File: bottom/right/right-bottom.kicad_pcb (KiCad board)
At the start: 2 copper layers, 171 x 95 mm, 6 parts

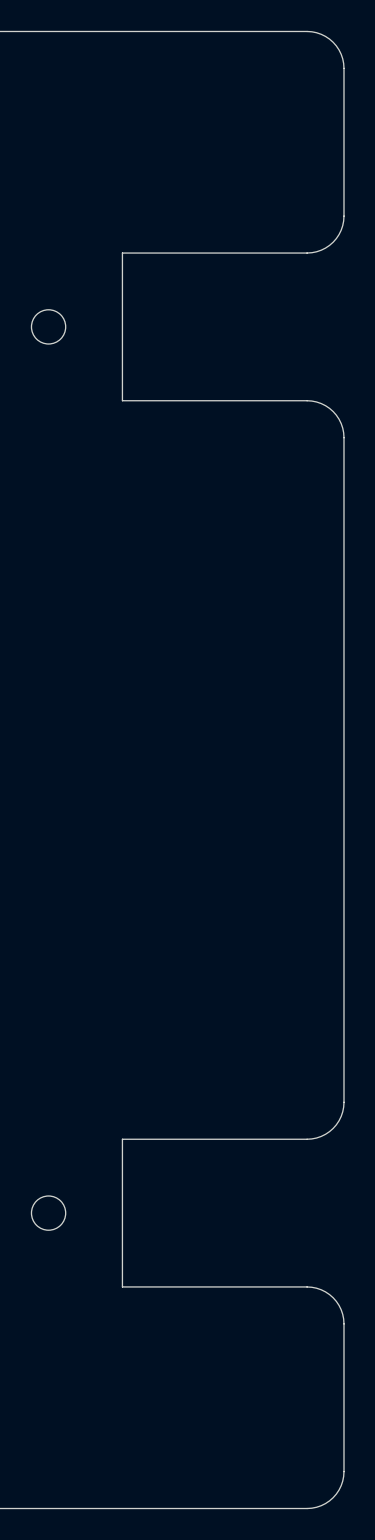
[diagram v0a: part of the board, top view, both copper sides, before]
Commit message: shlink cutout
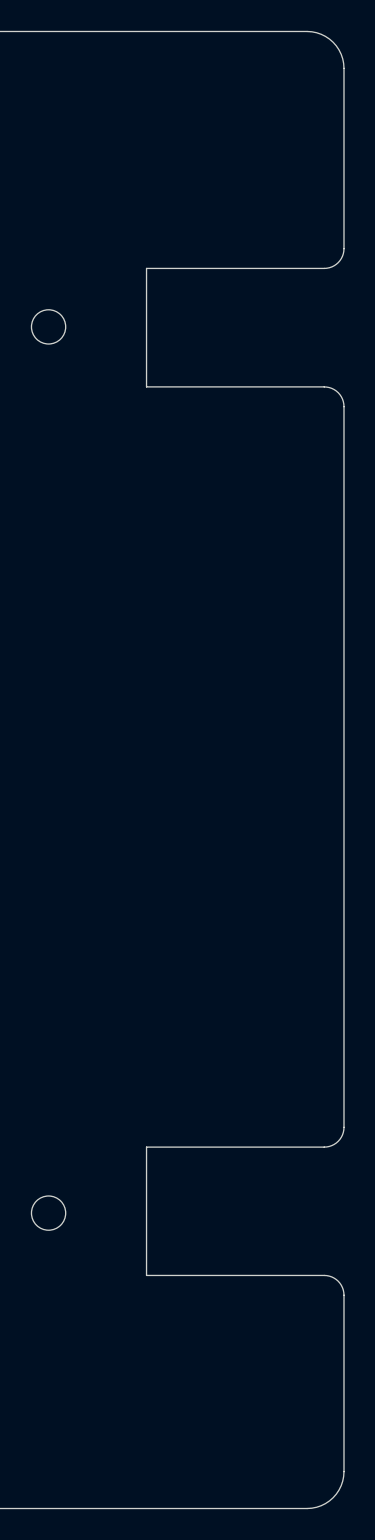
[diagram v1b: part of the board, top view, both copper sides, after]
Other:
- outline, holes or cut-outs redrawn
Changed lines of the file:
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@@
     (solder_mask_min_width 0.25)
     (aux_axis_origin 0 0)
+    (grid_origin 209 45.125)
     (visible_elements FFFFFF7F)
     (pcbplotparams
@@
     (pad 1 np_thru_hole circle (at 0 0) (size 2.2 2.2) (drill 2.2) (layers *.Cu *.Mask))
   )
-  (gr_arc (start 206.625 114) (end 206.625 116.375) (angle -90) (layer Edge.Cuts) (width 0.05))
-  (gr_arc (start 206.625 128.25) (end 209 128.25) (angle -90) (layer Edge.Cuts) (width 0.05))
-  (gr_line (start 209 137.75) (end 209 128.25) (layer Edge.Cuts) (width 0.05))
-  (gr_line (start 194.75 116.375) (end 206.625 116.375) (layer Edge.Cuts) (width 0.05))
-  (gr_line (start 194.75 125.875) (end 194.75 116.375) (layer Edge.Cuts) (width 0.05))
-  (gr_line (start 206.625 125.875) (end 194.75 125.875) (layer Edge.Cuts) (width 0.05))
-  (gr_arc (start 206.625 57) (end 206.625 59.375) (angle -90) (layer Edge.Cuts) (width 0.05))
-  (gr_arc (start 206.625 71.25) (end 209 71.25) (angle -90) (layer Edge.Cuts) (width 0.05))
-  (gr_line (start 209 47.5) (end 209 57) (layer Edge.Cuts) (width 0.05))
-  (gr_line (start 194.75 68.875) (end 206.625 68.875) (layer Edge.Cuts) (width 0.05))
-  (gr_line (start 194.75 59.375) (end 194.75 68.875) (layer Edge.Cuts) (width 0.05))
-  (gr_line (start 206.625 59.375) (end 194.75 59.375) (layer Edge.Cuts) (width 0.05))
+  (gr_arc (start 207.73 115.61) (end 207.73 116.88) (angle -90) (layer Edge.Cuts) (width 0.05))
+  (gr_arc (start 207.73 126.405) (end 209 126.405) (angle -90) (layer Edge.Cuts) (width 0.05))
+  (gr_arc (start 207.73 69.255) (end 209 69.255) (angle -90) (layer Edge.Cuts) (width 0.05))
+  (gr_arc (start 207.73 59.095) (end 207.73 60.365) (angle -90) (layer Edge.Cuts) (width 0.05))
+  (gr_line (start 209 137.75) (end 209 126.405) (layer Edge.Cuts) (width 0.05))
+  (gr_line (start 196.3 116.88) (end 207.73 116.88) (layer Edge.Cuts) (width 0.05))
+  (gr_line (start 196.3 125.135) (end 196.3 116.88) (layer Edge.Cuts) (width 0.05))
+  (gr_line (start 207.73 125.135) (end 196.3 125.135) (layer Edge.Cuts) (width 0.05))
+  (gr_line (start 209 47.5) (end 209 59.095) (layer Edge.Cuts) (width 0.05))
+  (gr_line (start 196.3 67.985) (end 207.73 67.985) (layer Edge.Cuts) (width 0.05))
+  (gr_line (start 196.3 60.365) (end 196.3 67.985) (layer Edge.Cuts) (width 0.05))
+  (gr_line (start 207.73 60.365) (end 196.3 60.365) (layer Edge.Cuts) (width 0.05))
   (gr_line (start 66.5 45.125) (end 40.375 45.125) (layer Edge.Cuts) (width 0.05))
   (gr_arc (start 59.375 137.75) (end 57 137.75) (angle -90) (layer Edge.Cuts) (width 0.05))
@@
   (gr_line (start 61.75 121.125) (end 59.375 121.125) (layer Edge.Cuts) (width 0.05))
   (gr_line (start 57 137.75) (end 57 123.5) (layer Edge.Cuts) (width 0.05))
-  (gr_line (start 209 71.25) (end 209 114) (layer Edge.Cuts) (width 0.05))
+  (gr_line (start 209 69.255) (end 209 115.61) (layer Edge.Cuts) (width 0.05))
   (gr_line (start 66.5 45.125) (end 206.625 45.125) (layer Edge.Cuts) (width 0.05))
   (gr_line (start 38 61.75) (end 38 47.5) (layer Edge.Cuts) (width 0.05))

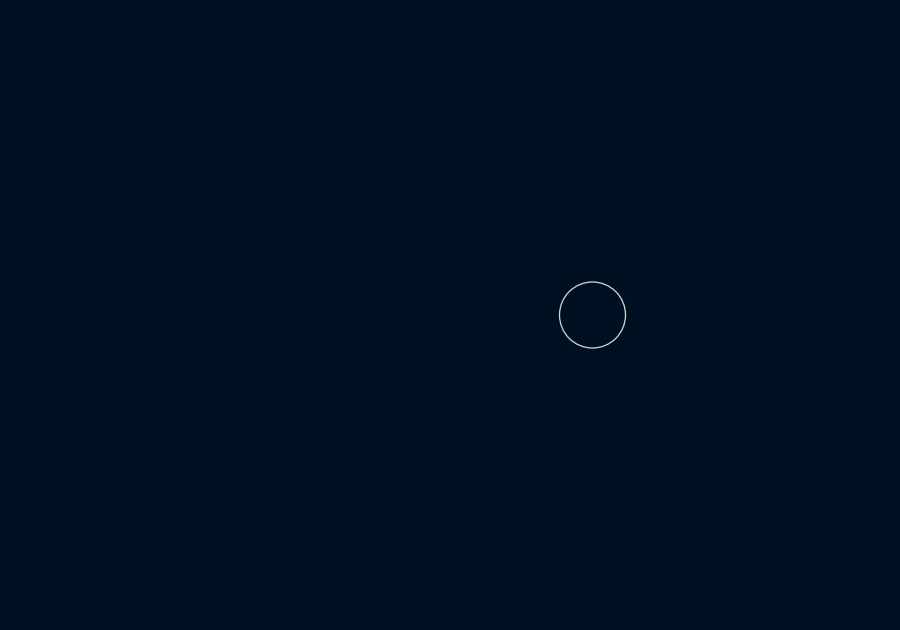
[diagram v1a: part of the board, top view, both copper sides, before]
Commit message: move right drillhole
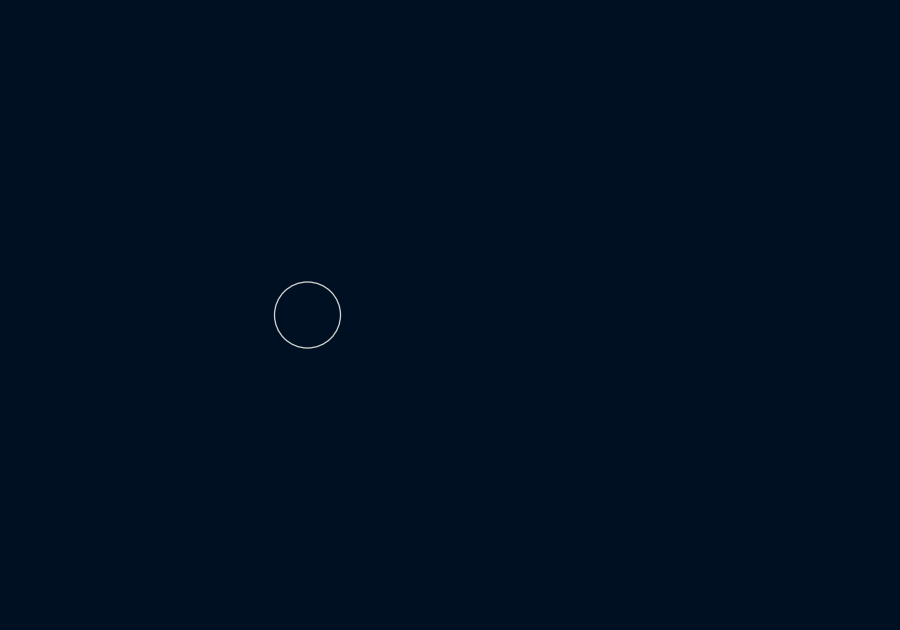
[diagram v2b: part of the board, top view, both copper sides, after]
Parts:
- moved ? 9.50 mm to (118.8, 121.1)
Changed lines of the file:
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@@
   )
   (module lib:MountingHole_2.2mm_M2 locked (layer F.Cu)
-    (at 128.25 121.125)
+    (at 118.75 121.125)
     (descr "Mounting Hole 2.2mm, no annular, M2")
     (tags "mounting hole 2.2mm no annular m2")

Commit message: move screw holl
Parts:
- moved ? 4.75 mm to (185.2, 121.1)
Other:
- board text added: "Satsuma JP SMD bottom plate rev.1"
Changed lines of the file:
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@@
   (general
     (thickness 1.6)
-    (drawings 35)
+    (drawings 36)
     (tracks 0)
     (zones 0)
@@
   )
   (module lib:MountingHole_2.2mm_M2 locked (layer F.Cu)
-    (at 190 121.125)
+    (at 185.25 121.125)
     (descr "Mounting Hole 2.2mm, no annular, M2")
     (tags "mounting hole 2.2mm no annular m2")
@@
     (pad 1 np_thru_hole circle (at 0 0) (size 2.2 2.2) (drill 2.2) (layers *.Cu *.Mask))
   )
+  (gr_text "Satsuma JP SMD bottom plate rev.1" (at 184.235 136.565) (layer F.SilkS)
+    (effects (font (size 1.5 1.5) (thickness 0.3)))
+  )
   (gr_arc (start 207.73 115.61) (end 207.73 116.88) (angle -90) (layer Edge.Cuts) (width 0.05))
